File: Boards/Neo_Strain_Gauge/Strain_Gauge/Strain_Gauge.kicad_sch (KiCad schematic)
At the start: 59 parts, among them J1 Screw_Terminal_01x03, J2 Screw_Terminal_01x03, J3 Screw_Terminal_01x03, J4 Screw_Terminal_01x03, J5 Conn_01x02, J6 USB_B_Micro, J7 Conn_02x10_Counter_Clockwise, J8 Conn_02x12_Counter_Clockwise, U1 W25Q128JVS, U2 NCP1117-3.3_SOT223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

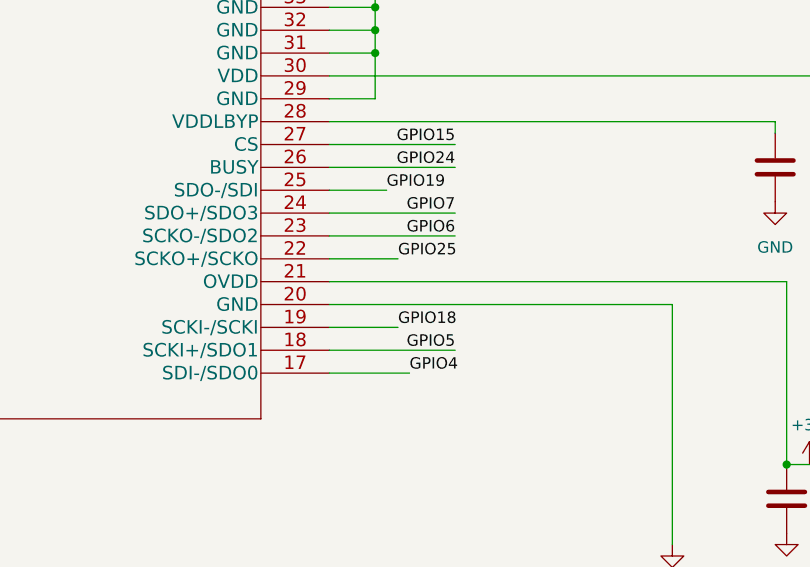
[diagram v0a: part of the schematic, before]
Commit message: It's apparently possible to communicate over SPI to the ADC
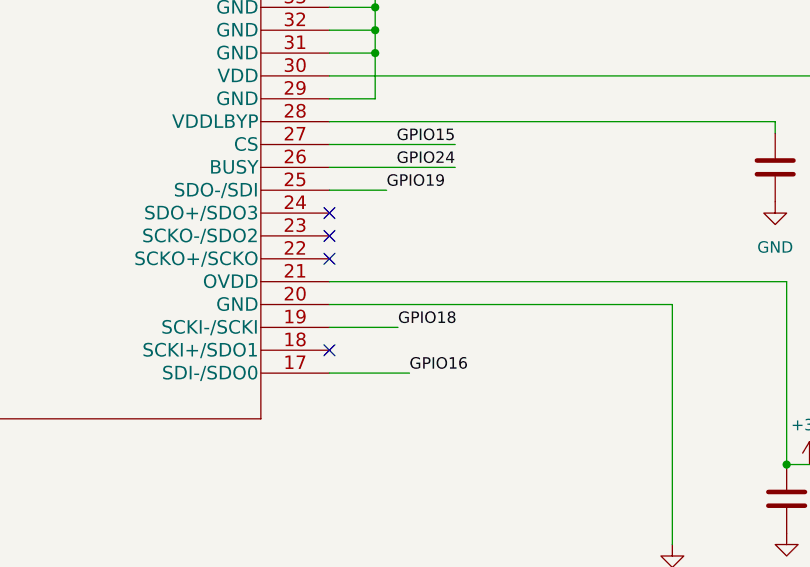
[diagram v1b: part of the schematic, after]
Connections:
- net GPIO16: now also U3.17 (SDI-/SDO0)
- net GPIO25: no longer U3.22 (SCKO+/SCKO)
- net GPIO4: no longer U3.17 (SDI-/SDO0)
- net GPIO5: no longer U3.18 (SCKI+/SDO1)
- net GPIO6: no longer U3.23 (SCKO-/SDO2)
- net GPIO7: no longer U3.24 (SDO+/SDO3)
- no-connect marks 2 -> 6
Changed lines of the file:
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@@
   (junction (at 368.3 284.48) (diameter 0) (color 0 0 0 0)
   )
+  (no_connect (at 25.4 294.64))
+  (no_connect (at 25.4 297.18))
+  (no_connect (at 25.4 299.72))
+  (no_connect (at 25.4 309.88))
   (no_connect (at 233.68 273.05))
   (no_connect (at 152.4 351.79))
@@
     (stroke (width 0) (type default) (color 0 0 0 0))
   )
-  (wire (pts (xy 39.37 297.18) (xy 25.4 297.18))
-    (stroke (width 0) (type default) (color 0 0 0 0))
-  )
   (wire (pts (xy -228.6 327.66) (xy -228.6 344.17))
     (stroke (width 0) (type default) (color 0 0 0 0))
@@
     (stroke (width 0) (type default) (color 0 0 0 0))
   )
-  (wire (pts (xy 39.37 294.64) (xy 25.4 294.64))
-    (stroke (width 0) (type default) (color 0 0 0 0))
-  )
   (wire (pts (xy 441.96 264.16) (xy 453.39 264.16))
     (stroke (width 0) (type default) (color 0 0 0 0))
@@
     (stroke (width 0) (type default) (color 0 0 0 0))
   )
-  (wire (pts (xy 25.4 299.72) (xy 33.02 299.72))
-    (stroke (width 0) (type default) (color 0 0 0 0))
-  )
   (wire (pts (xy 391.16 355.6) (xy 406.4 355.6))
     (stroke (width 0) (type default) (color 0 0 0 0))
@@
   )
   (wire (pts (xy -222.25 284.48) (xy -217.17 284.48))
-    (stroke (width 0) (type default) (color 0 0 0 0))
-  )
-  (wire (pts (xy 39.37 309.88) (xy 25.4 309.88))
     (stroke (width 0) (type default) (color 0 0 0 0))
   )
@@
     (effects (font (size 1.27 1.27)) (justify left bottom))
   )
-  (label "GPIO7" (at 39.37 294.64 180)
-    (effects (font (size 1.27 1.27)) (justify right bottom))
-  )
   (label "USB_DR+" (at 397.51 304.8 0)
     (effects (font (size 1.27 1.27)) (justify left bottom))
@@
     (effects (font (size 1.27 1.27)) (justify left bottom))
   )
-  (label "GPIO5" (at 39.37 309.88 180)
-    (effects (font (size 1.27 1.27)) (justify right bottom))
-  )
   (label "QSPI_SCLK" (at 215.9 334.01 0)
     (effects (font (size 1.27 1.27)) (justify left bottom))
@@
     (effects (font (size 1.27 1.27)) (justify right bottom))
   )
-  (label "GPIO6" (at 39.37 297.18 180)
-    (effects (font (size 1.27 1.27)) (justify right bottom))
-  )
   (label "rpi_gpio11" (at 101.6 367.03 0)
     (effects (font (size 1.27 1.27)) (justify left bottom))
@@
     (effects (font (size 1.27 1.27)) (justify left bottom))
   )
-  (label "GPIO4" (at 34.29 312.42 0)
+  (label "GPIO16" (at 34.29 312.42 0)
     (effects (font (size 1.27 1.27)) (justify left bottom))
   )
@@
     (effects (font (size 1.27 1.27)) (justify left bottom))
   )
-  (label "GPIO25" (at 33.02 299.72 0)
-    (effects (font (size 1.27 1.27)) (justify left bottom))
-  )

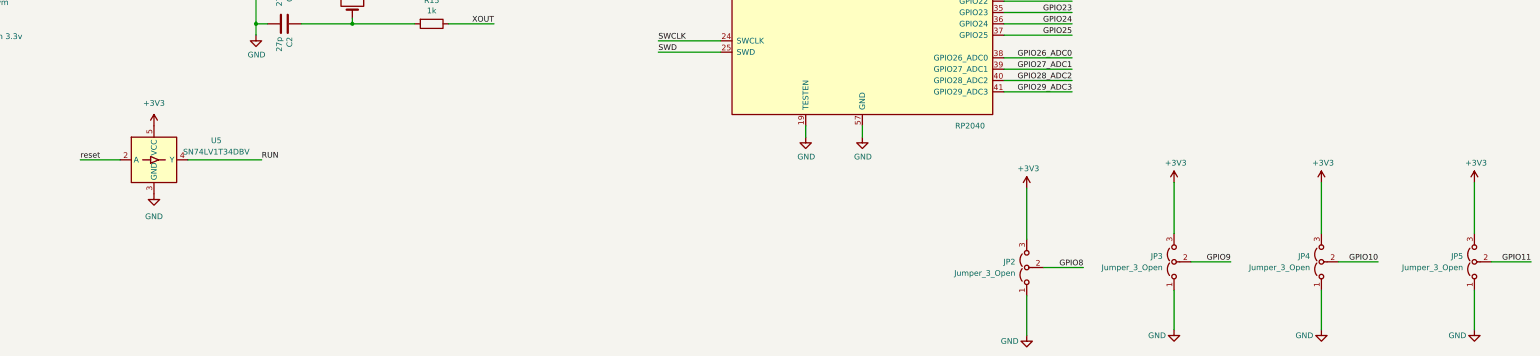
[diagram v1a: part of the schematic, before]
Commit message: More micro-adjustments and add the I2C lines
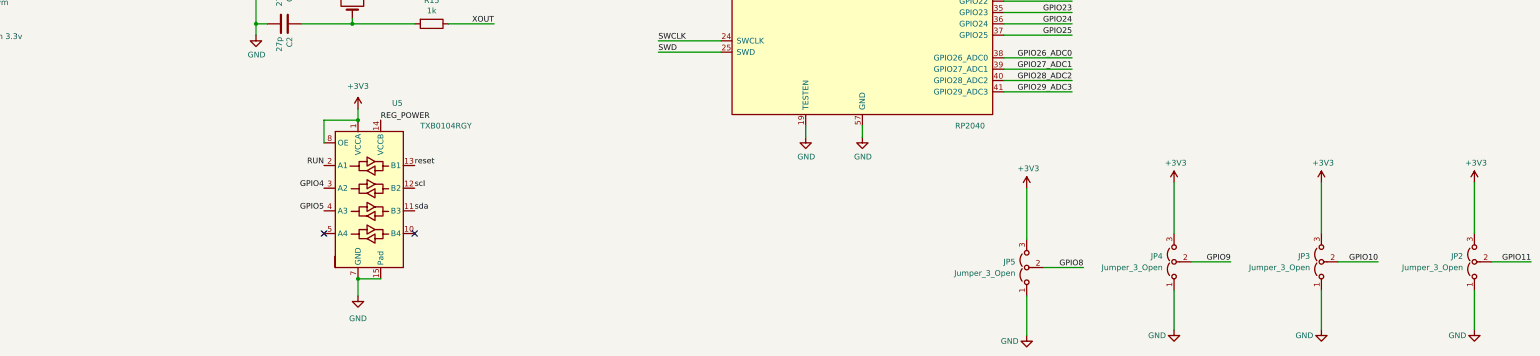
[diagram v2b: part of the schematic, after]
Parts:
- removed U5: SN74LV1T34DBV, Package_TO_SOT_SMD:SOT-23-5, symbol Logic_LevelTranslator:SN74LV1T34DBV
- added U5: TXB0104RGY, Package_DFN_QFN:Texas_S-PVQFN-N14, symbol Logic_LevelTranslator:TXB0104RGY
- R13, R15: Purchase Link (none) -> https://www.digikey.com/en/products/detail/stackpole-electr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
- U1: Purchase Link (none) -> https://www.digikey.com/en/products/detail/winbond-electron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
- U2: Purchase Link (none) -> https://www.digikey.com/en/products/detail/onsemi/NCP1117LP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
- U3: Purchase Link (none) -> https://www.digikey.com/en/products/detail/analog-devices-i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
- U4: Purchase Link (none) -> https://www.digikey.com/en/products/detail/raspberry-pi/SC0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
- renumbered JP5 to JP2, JP4 to JP3, JP3 to JP4, JP2 to JP5
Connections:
- net +3V3: now also U5.1 (VCCA), U5.8 (OE)
- net GND: now also U5.15 (Pad), U5.7 (GND)
- net GPIO4: now also U5.3 (A2)
- net GPIO5: now also U5.4 (A3)
- net REG_POWER: now also U5.14 (VCCB)
- net RUN: now also U5.2 (A1)
- net reset: now also U5.13 (B1)
- net scl: now also U5.12 (B2)
- net sda: now also U5.11 (B3)
- no-connect marks 6 -> 8

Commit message: Anti-emi Aktion
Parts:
- C20: Purchase Link (none) -> https://www.digikey.com/en/products/detail/samsung-electro-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
- J7: Purchase Link (none) -> https://www.digikey.com/en/products/detail/adam-tech/RS2-20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
- R3, R4: Purchase Link (none) -> https://www.digikey.com/en/products/detail/rohm-semiconduct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
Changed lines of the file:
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@@
+      (effects (font (size 1.27 1.27)) hide)
+    )
+    (property "Purchase Link" "https://www.digikey.com/en/products/detail/rohm-semiconductor/ESR01MZPJ270/16180022" (id 4) (at 406.4 307.34 0)
       (effects (font (size 1.27 1.27)) hide)
     )
@@
       (effects (font (size 1.27 1.27)) hide)
     )
+    (property "Purchase Link" "https://www.digikey.com/en/products/detail/rohm-semiconductor/ESR01MZPJ270/16180022" (id 4) (at 406.4 299.72 0)
+      (effects (font (size 1.27 1.27)) hide)
+    )
     (pin "1")
     (pin "2")
@@
     )
     (property "Datasheet" "~" (id 3) (at 267.97 238.76 0)
+      (effects (font (size 1.27 1.27)) hide)
+    )
+    (property "Purchase Link" "https://www.digikey.com/en/products/detail/samsung-electro-mechanics/CL10A226MP8NUNE/3886932" (id 4) (at 267.97 238.76 0)
       (effects (font (size 1.27 1.27)) hide)
     )
@@
       (effects (font (size 1.27 1.27)) hide)
     )
+    (property "Purchase Link" "https://www.digikey.com/en/products/detail/adam-tech/RS2-20-G/9832051" (id 4) (at 93.98 359.41 0)
+      (effects (font (size 1.27 1.27)) hide)
+    )

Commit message: Micro-optimized it all.
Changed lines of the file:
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@@
   (junction (at 30.48 274.32) (diameter 0) (color 0 0 0 0)
   )
-  (junction (at 30.48 271.78) (diameter 0) (color 0 0 0 0)
-  )
   (junction (at 241.3 232.41) (diameter 0) (color 0 0 0 0)
   )
@@
     (stroke (width 0) (type default) (color 0 0 0 0))
   )
-  (wire (pts (xy 30.48 256.54) (xy 30.48 271.78))
-    (stroke (width 0) (type default) (color 0 0 0 0))
-  )
   (wire (pts (xy 346.71 284.48) (xy 341.63 284.48))
     (stroke (width 0) (type default) (color 0 0 0 0))
@@
     (pin "1")
   )
-  (symbol (lib_id "power:GND") (at 30.48 256.54 90) (unit 1)
-    (in_bom yes) (on_board yes) (fields_autoplaced)
-    (property "Reference" "#PWR0108" (id 0) (at 36.83 256.54 0)
-      (effects (font (size 1.27 1.27)) hide)
-    )
-    (property "Value" "GND" (id 1) (at 34.29 256.5399 90)
-      (effects (font (size 1.27 1.27)) (justify right))
-    )
-    (property "Footprint" "" (id 2) (at 30.48 256.54 0)
-      (effects (font (size 1.27 1.27)) hide)
-    )
-    (property "Datasheet" "" (id 3) (at 30.48 256.54 0)
-      (effects (font (size 1.27 1.27)) hide)
-    )
-    (pin "1")
-  )
   (symbol (lib_id "power:GND") (at -53.34 316.23 0) (unit 1)
     (in_bom yes) (on_board yes) (fields_autoplaced)
@@
     (pin "1")
   )
+  (symbol (lib_id "power:GND") (at 30.48 276.86 90) (unit 1)
+    (in_bom yes) (on_board yes) (fields_autoplaced)
+    (property "Reference" "#PWR?" (id 0) (at 36.83 276.86 0)
+      (effects (font (size 1.27 1.27)) hide)
+    )
+    (property "Value" "GND" (id 1) (at 34.29 276.8599 90)
+      (effects (font (size 1.27 1.27)) (justify right))
+    )
+    (property "Footprint" "" (id 2) (at 30.48 276.86 0)
+      (effects (font (size 1.27 1.27)) hide)
+    )
+    (property "Datasheet" "" (id 3) (at 30.48 276.86 0)
+      (effects (font (size 1.27 1.27)) hide)
+    )
+    (pin "1")
+  )
   (symbol (lib_id "Device:C") (at 441.96 269.24 0) (unit 1)
     (in_bom yes) (on_board yes)
@@
       (reference "#PWR0107") (unit 1) (value "+3V3") (footprint "")
     )
-    (path "/9319553c-0309-4662-b965-569ef111628a"
-      (reference "#PWR0108") (unit 1) (value "GND") (footprint "")
-    )
     (path "/88baf129-7bef-4b9b-9935-3a1fa9347d27"
       (reference "#PWR0109") (unit 1) (value "GND") (footprint "")
@@
       (reference "#PWR0138") (unit 1) (value "GND") (footprint "")
     )
+    (path "/d7cc4ae9-bbfe-4970-952d-33b11227f81c"
+      (reference "#PWR?") (unit 1) (value "GND") (footprint "")
+    )
     (path "/5ada49b8-8e96-4086-b7e6-4acbf8622b7e"

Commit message: Swap what we use for the SPI pins to make routing slightly better
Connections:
- net GPIO1: now also U3.27 (CS)
- net GPIO15: no longer U3.27 (CS)
- net GPIO16: no longer U3.17 (SDI-/SDO0)
- net GPIO18: no longer U3.19 (SCKI-/SCKI)
- net GPIO19: no longer U3.25 (SDO-/SDI)
- net GPIO2: now also U3.19 (SCKI-/SCKI)
- net GPIO28_ADC2: now also U5.4 (A3)
- net GPIO29_ADC3: now also U5.3 (A2)
- net GPIO3: now also U3.25 (SDO-/SDI)
- net GPIO4: now also U3.17 (SDI-/SDO0); no longer U5.3 (A2)
- net GPIO5: no longer U5.4 (A3)
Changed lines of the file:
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@@
     (effects (font (size 1.27 1.27)) (justify right bottom))
   )
-  (label "GPIO5" (at 238.76 417.83 180)
+  (label "GPIO28_ADC2" (at 238.76 417.83 180)
     (effects (font (size 1.27 1.27)) (justify right bottom))
   )
@@
     (effects (font (size 1.27 1.27)) (justify right bottom))
   )
-  (label "GPIO18" (at 33.02 307.34 0)
+  (label "GPIO2" (at 33.02 307.34 0)
     (effects (font (size 1.27 1.27)) (justify left bottom))
   )
@@
     (effects (font (size 1.27 1.27)) (justify left bottom))
   )
-  (label "GPIO15" (at 39.37 287.02 180)
+  (label "GPIO1" (at 39.37 287.02 180)
     (effects (font (size 1.27 1.27)) (justify right bottom))
   )
@@
     (effects (font (size 1.27 1.27)) (justify right bottom))
   )
-  (label "GPIO19" (at 31.75 292.1 0)
+  (label "GPIO3" (at 31.75 292.1 0)
     (effects (font (size 1.27 1.27)) (justify left bottom))
   )
@@
     (effects (font (size 1.27 1.27)) (justify left bottom))
   )
-  (label "GPIO4" (at 238.76 412.75 180)
+  (label "GPIO29_ADC3" (at 238.76 412.75 180)
     (effects (font (size 1.27 1.27)) (justify right bottom))
   )
@@
     (effects (font (size 1.27 1.27)) (justify left bottom))
   )
-  (label "GPIO16" (at 34.29 312.42 0)
-    (effects (font (size 1.27 1.27)) (justify left bottom))
-  )
+  (label "GPIO4" (at 34.29 312.42 0)
+    (effects (font (size 1.27 1.27)) (justify left bottom))
+  )

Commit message: Filter the voltage input to the system
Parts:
- added C24, C27, C28, C29: 0.1pF, Capacitor_SMD:C_0603_1608Metric, symbol Device:C
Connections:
- net +5V: now also C24.2, C27.2, C28.2, C29.2
- net GND: now also C24.1, C27.1, C28.1, C29.1
